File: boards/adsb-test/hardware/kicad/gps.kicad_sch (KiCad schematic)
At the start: 0 parts

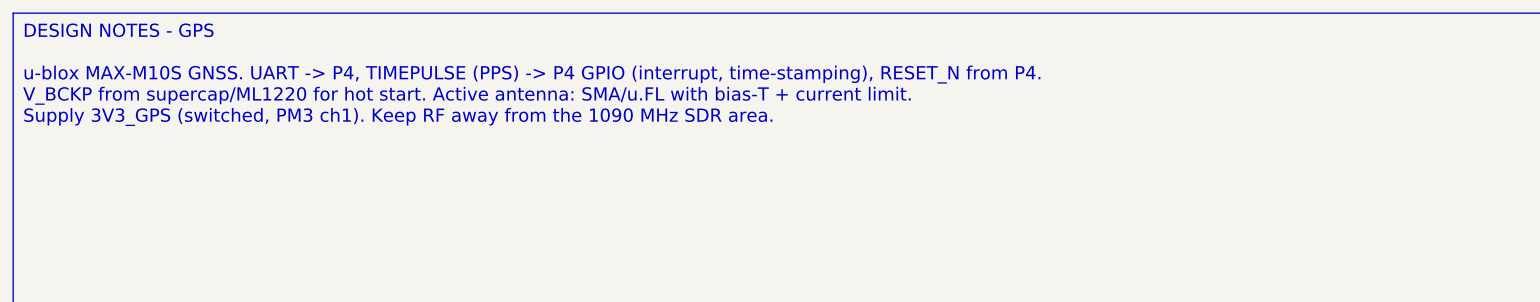
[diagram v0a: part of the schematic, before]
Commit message: Release v0.4.0: ADSB_Test with ESP32-C5, ADSBee m1421 and LA5016 header
- C6 -> C5 co-processor; m1421 identified and integrated (symbol/footprint
  from the ADSBee 1421 carrier, GPL-3.0 attribution)
- Power budget and 2S1P battery sizing for >= 1 h; USB-A for 1-2 SDRs via hub
- Dev port: FT2232H + RP2040 debugprobe; TCA6408A expander for slow I/O
- Test Debug sheet with LA5016 header and rail test points
- Vendor documents git-ignored (public repo)

Co-Authored-By: Claude Opus 5.5 <noreply@anthropic.com>
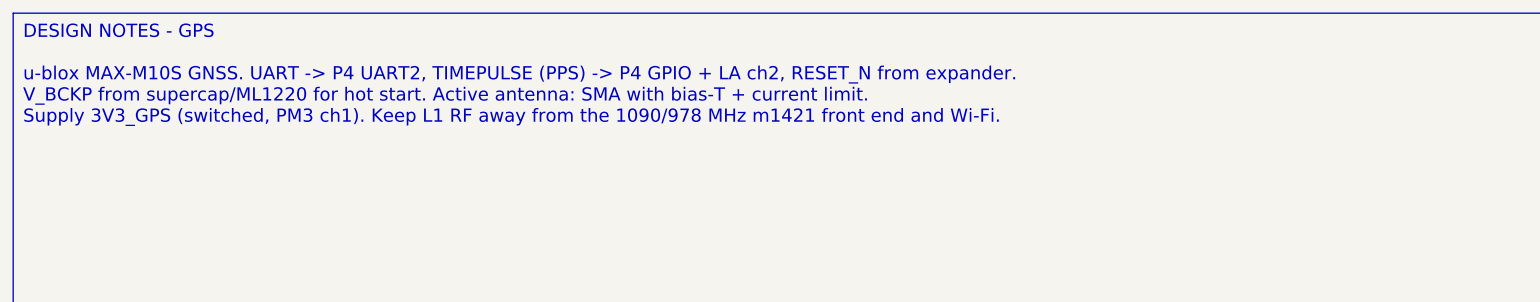
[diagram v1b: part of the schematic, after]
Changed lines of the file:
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@@
 		(comment 1 "Requirements: boards/adsb-test/docs/requirements.md")
 	)
-	(text_box "DESIGN NOTES - GPS\n\nu-blox MAX-M10S GNSS. UART -> P4, TIMEPULSE (PPS) -> P4 GPIO (interrupt, time-stamping), RESET_N from P4.\nV_BCKP from supercap/ML1220 for hot start. Active antenna: SMA/u.FL with bias-T + current limit.\nSupply 3V3_GPS (switched, PM3 ch1). Keep RF away from the 1090 MHz SDR area."
+	(text_box "DESIGN NOTES - GPS\n\nu-blox MAX-M10S GNSS. UART -> P4 UART2, TIMEPULSE (PPS) -> P4 GPIO + LA ch2, RESET_N from expander.\nV_BCKP from supercap/ML1220 for hot start. Active antenna: SMA with bias-T + current limit.\nSupply 3V3_GPS (switched, PM3 ch1). Keep L1 RF away from the 1090/978 MHz m1421 front end and Wi-Fi."
 		(exclude_from_sim no)
 		(at 20 20 0)
